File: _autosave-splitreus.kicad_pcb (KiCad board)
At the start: 2 copper layers, 132.5 x 101 mm, 73 parts, among them J1 TRRS, J2 LED, SW0 SW_PUSH, SW1 SW_PUSH, SW10 SW_PUSH, SW11 SW_PUSH, SW12 SW_PUSH, SW13 SW_PUSH, SW14 SW_PUSH, SW15 SW_PUSH, SW16 SW_PUSH, SW17 SW_PUSH, SW18 SW_PUSH, SW19 SW_PUSH, SW2 SW_PUSH, SW20 SW_PUSH, SW21 SW_PUSH, SW22 SW_PUSH, SW23 SW_PUSH, SW24 SW_PUSH, SW25 SW_PUSH, SW26 SW_PUSH, SW27 SW_PUSH, SW28 SW_PUSH, SW29 SW_PUSH, SW3 SW_PUSH, SW30 SW_PUSH, SW4 SW_PUSH, SW5 SW_PUSH, SW6 SW_PUSH, SW7 SW_PUSH, SW8 SW_PUSH, SW9 SW_PUSH, U1 ProMicro, U2 HOLE, U3 HOLE, U4 HOLE, U5 HOLE, U6 HOLE

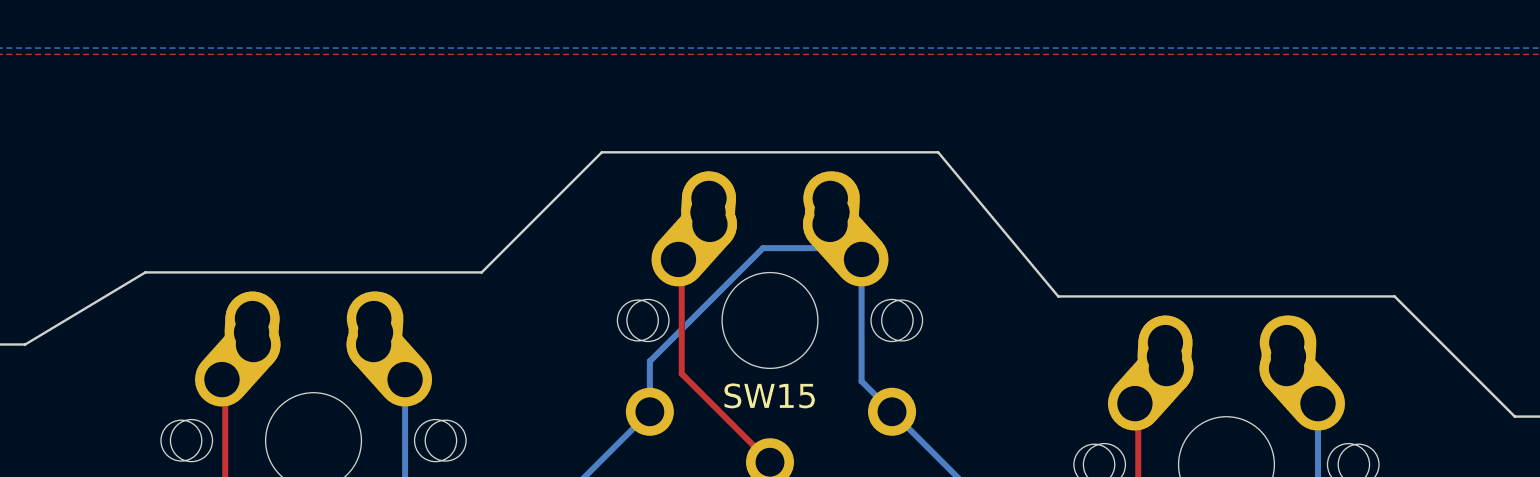
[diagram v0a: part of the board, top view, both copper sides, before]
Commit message: Untested, unverified mid mount trrs
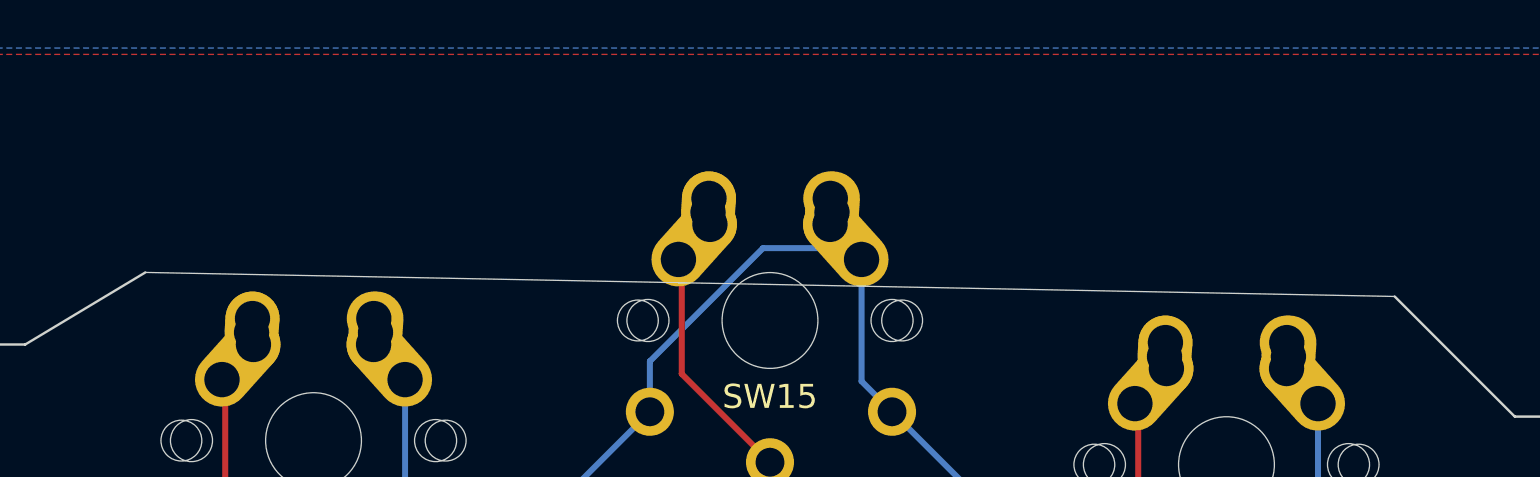
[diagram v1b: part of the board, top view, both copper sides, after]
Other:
- board size 132.5 x 101 mm -> 132.5 x 96 mm
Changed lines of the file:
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@@
   (general
     (thickness 1.6)
-    (drawings 460)
+    (drawings 456)
     (tracks 1197)
     (zones 0)
@@
   )
   (layers
-    (0 F.Cu signal)
-    (31 B.Cu signal)
-    (32 B.Adhes user)
-    (33 F.Adhes user)
-    (34 B.Paste user)
-    (35 F.Paste user)
-    (36 B.SilkS user)
-    (37 F.SilkS user)
-    (38 B.Mask user)
-    (39 F.Mask user)
-    (40 Dwgs.User user)
+    (0 F.Cu signal hide)
+    (31 B.Cu signal hide)
+    (32 B.Adhes user hide)
+    (33 F.Adhes user hide)
+    (34 B.Paste user hide)
+    (35 F.Paste user hide)
+    (36 B.SilkS user hide)
+    (37 F.SilkS user hide)
+    (38 B.Mask user hide)
+    (39 F.Mask user hide)
+    (40 Dwgs.User user hide)
     (41 Cmts.User user hide)
-    (42 Eco1.User user)
-    (43 Eco2.User user)
+    (42 Eco1.User user hide)
+    (43 Eco2.User user hide)
     (44 Edge.Cuts user)
-    (45 Margin user)
-    (46 B.CrtYd user)
-    (47 F.CrtYd user)
-    (48 B.Fab user)
-    (49 F.Fab user)
+    (45 Margin user hide)
+    (46 B.CrtYd user hide)
+    (47 F.CrtYd user hide)
+    (48 B.Fab user hide)
+    (49 F.Fab user hide)
   )
   (setup
@@
       (net 31 ROW0))
   )
+  (gr_line (start 83 -9) (end 30.999999 -10) (layer Edge.Cuts) (width 0.05))
   (gr_text R (at 117.55784 42.8854) (layer B.SilkS)
     (effects (font (size 1.5 1.5) (thickness 0.3)) (justify mirror))
@@
   (gr_arc (start -7 82.23125) (end -7.749999 82.4) (angle -77.31961651) (layer Edge.Cuts) (width 0.1))
   (gr_line (start 83 -9) (end 88 -4) (layer Edge.Cuts) (width 0.1))
-  (gr_line (start 64 -15) (end 69 -9) (layer Edge.Cuts) (width 0.1))
-  (gr_line (start 44.999999 -10) (end 50 -15) (layer Edge.Cuts) (width 0.1))
   (gr_line (start 26 -7) (end 30.999999 -10) (layer Edge.Cuts) (width 0.1))
   (gr_line (start 7 -7) (end 12 -7) (layer Edge.Cuts) (width 0.1))
@@
   (gr_line (start 102.75 -3.4) (end 102.75 9.4) (layer Edge.Cuts) (width 0.1))
   (gr_line (start 88 -4) (end 102 -4) (layer Edge.Cuts) (width 0.1))
-  (gr_line (start 69 -9) (end 83 -9) (layer Edge.Cuts) (width 0.1))
-  (gr_line (start 50 -15) (end 64 -15) (layer Edge.Cuts) (width 0.1))
-  (gr_line (start 30.999999 -10) (end 44.999999 -10) (layer Edge.Cuts) (width 0.1))
   (gr_line (start 12 -7) (end 26 -7) (layer Edge.Cuts) (width 0.1))
   (gr_line (start 44.999999 80) (end 30.999999 80) (layer Edge.Cuts) (width 0.1))
